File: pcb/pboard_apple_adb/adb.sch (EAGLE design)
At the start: 25 parts, among them IC3 STM32F042F4, SW1 324_SW, SW2 324_SW, SW4 324_SW

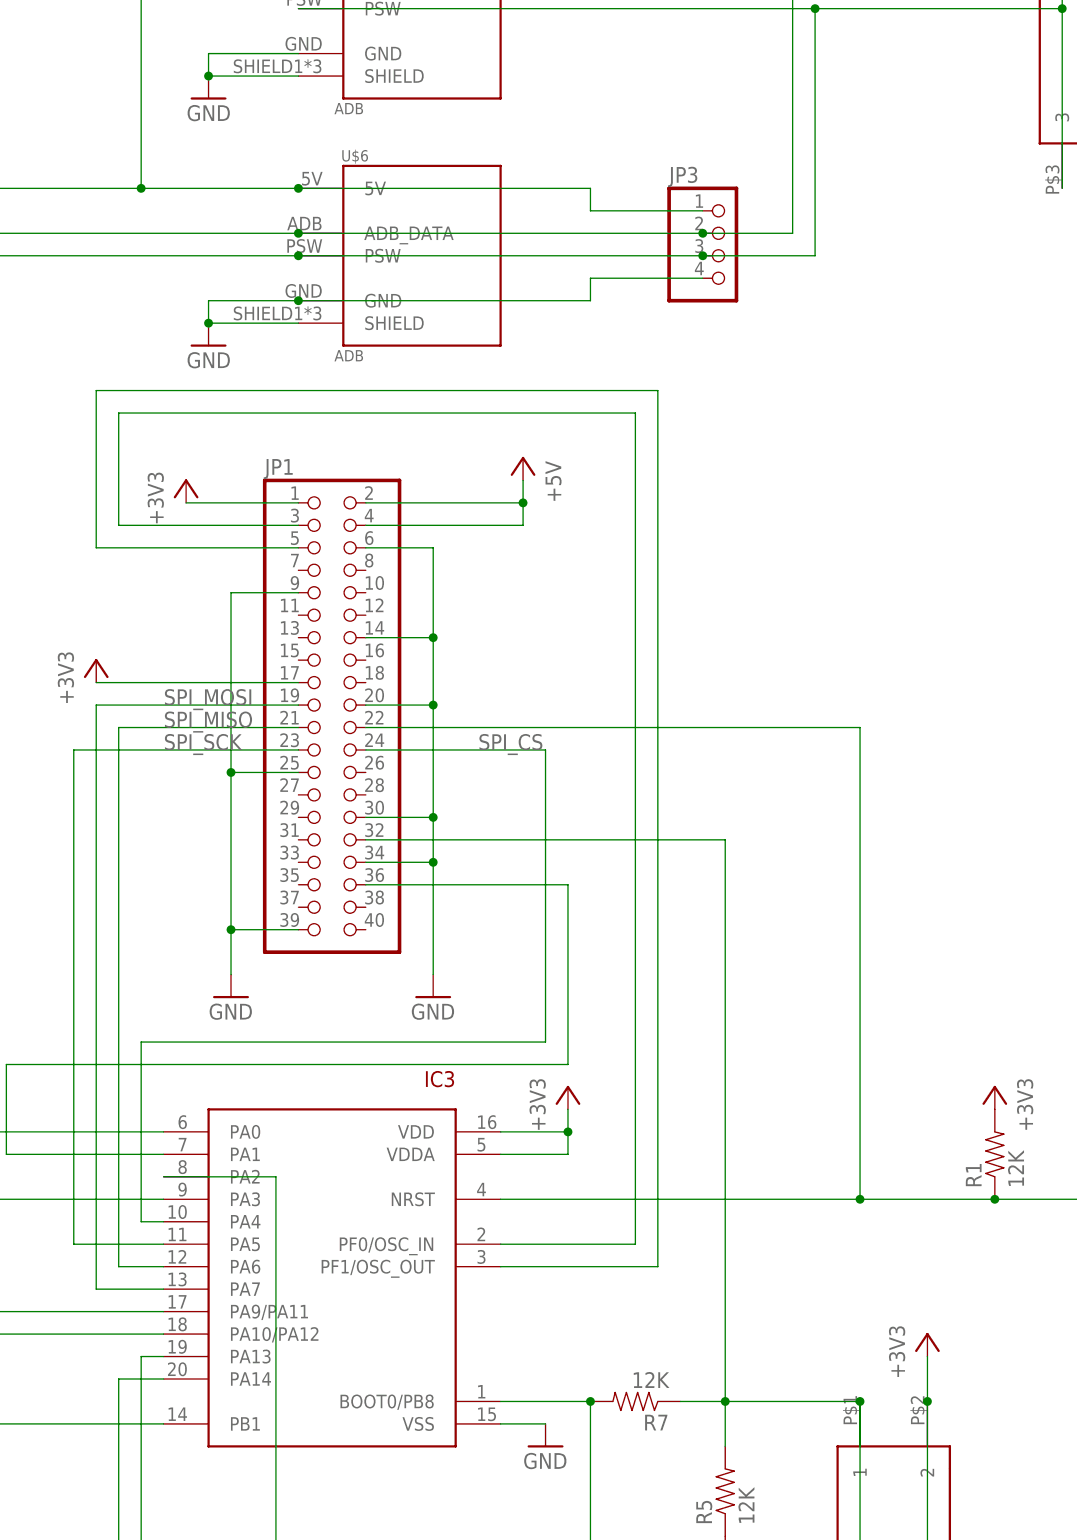
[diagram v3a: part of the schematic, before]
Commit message: updated PCB for second prototype run
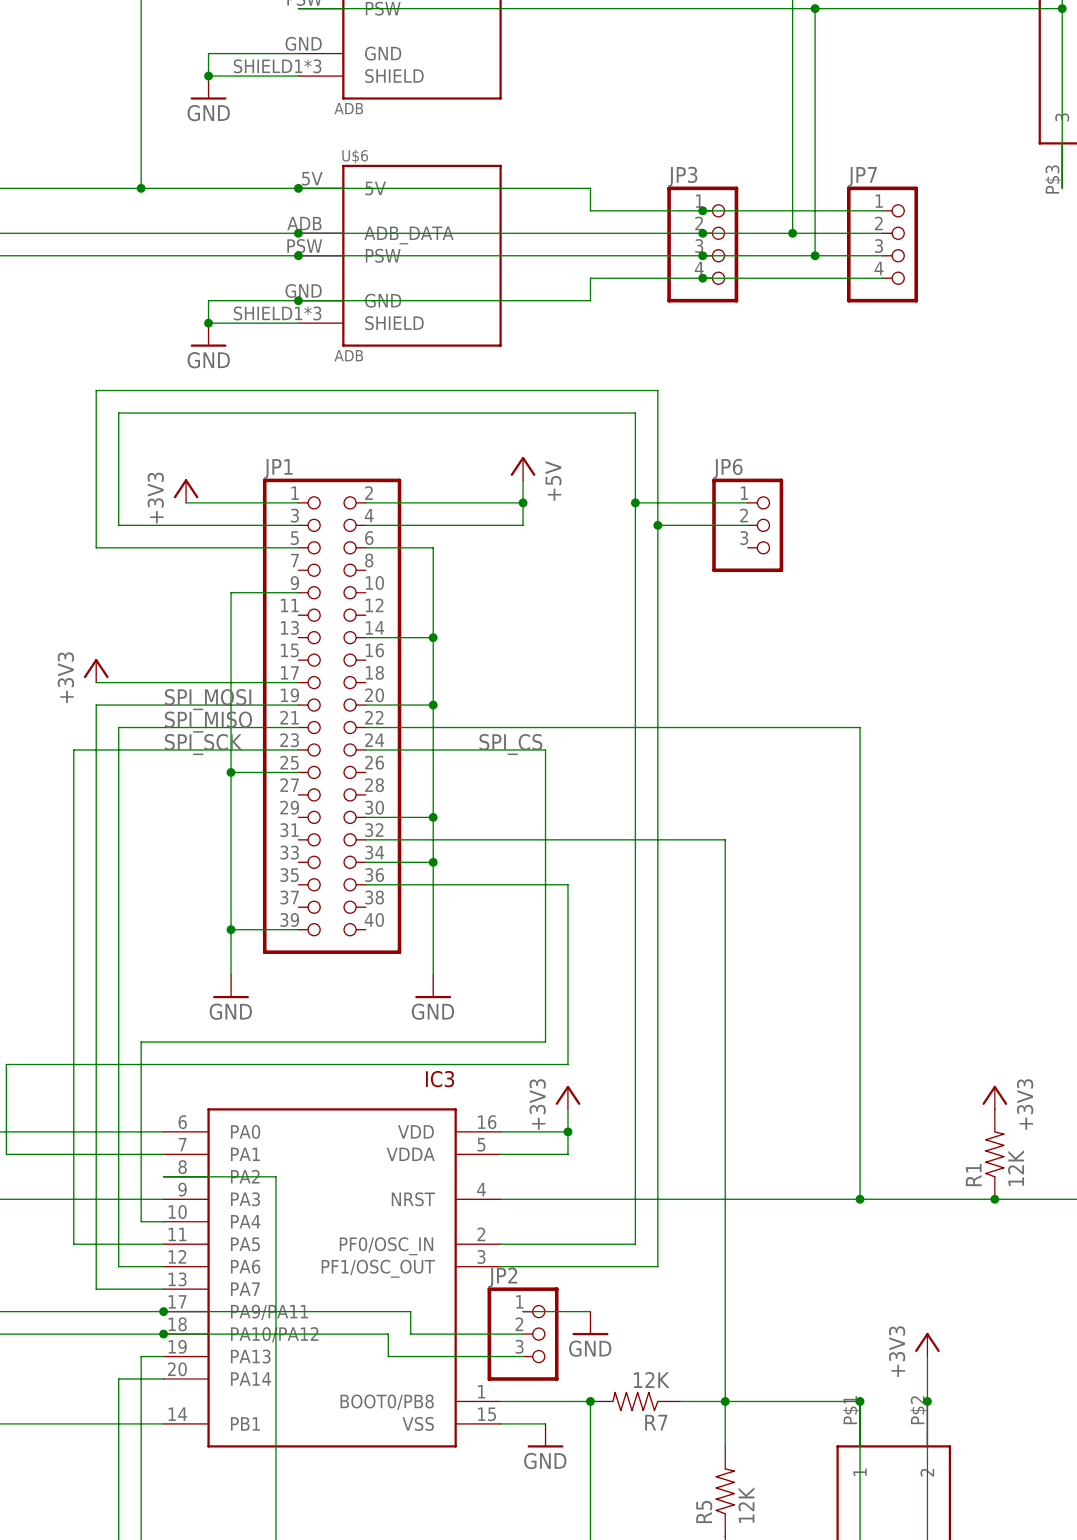
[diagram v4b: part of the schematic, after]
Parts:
- added JP2, JP6: (no value), pinhead:PINHD-1X3
- added JP7: (no value), pinhead:PINHD-1X4
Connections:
- net GND: now also JP2.1, JP7.4
- net N$10: now also JP6.1
- net N$11: now also JP6.2
- net N$14: now also JP7.1
- net N$15: now also JP7.2
- net N$18: now also JP7.3
- net N$3: now also JP2.3
- net N$4: now also JP2.2
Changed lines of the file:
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@@
 <part name="JP5" library="pinhead" library_urn="urn:adsk.eagle:library:325" deviceset="PINHD-1X5" device="" package3d_urn="urn:adsk.eagle:package:22469/2"/>
 <part name="R7" library="SparkFun-Passives" deviceset="RESISTOR" device="0805-RES" value="12K"/>
+<part name="JP2" library="pinhead" library_urn="urn:adsk.eagle:library:325" deviceset="PINHD-1X3" device="" package3d_urn="urn:adsk.eagle:package:22458/2"/>
+<part name="GND14" library="supply1" library_urn="urn:adsk.eagle:library:371" deviceset="GND" device=""/>
+<part name="JP6" library="pinhead" library_urn="urn:adsk.eagle:library:325" deviceset="PINHD-1X3" device="" package3d_urn="urn:adsk.eagle:package:22458/2"/>
+<part name="JP7" library="pinhead" library_urn="urn:adsk.eagle:library:325" deviceset="PINHD-1X4" device="" package3d_urn="urn:adsk.eagle:package:22407/2"/>
 </parts>
 <sheets>
@@
 <attribute name="NAME" x="138.43" y="-120.8786" size="1.778" layer="95" rot="R180"/>
 <attribute name="VALUE" x="138.43" y="-116.078" size="1.778" layer="96" rot="R180"/>
+</instance>
+<instance part="JP2" gate="A" x="124.46" y="-111.76" smashed="yes">
+<attribute name="NAME" x="118.11" y="-106.045" size="1.778" layer="95"/>
+<attribute name="VALUE" x="118.11" y="-119.38" size="1.778" layer="96"/>
+</instance>
+<instance part="GND14" gate="1" x="129.54" y="-111.76" smashed="yes">
+<attribute name="VALUE" x="127" y="-114.3" size="1.778" layer="96"/>
+</instance>
+<instance part="JP6" gate="A" x="149.86" y="-20.32" smashed="yes">
+<attribute name="NAME" x="143.51" y="-14.605" size="1.778" layer="95"/>
+<attribute name="VALUE" x="143.51" y="-27.94" size="1.778" layer="96"/>
+</instance>
+<instance part="JP7" gate="A" x="165.1" y="10.16" smashed="yes">
+<attribute name="NAME" x="158.75" y="18.415" size="1.778" layer="95"/>
+<attribute name="VALUE" x="158.75" y="2.54" size="1.778" layer="96"/>
 </instance>
 </instances>
@@
 <junction x="96.52" y="5.08"/>
 <junction x="86.36" y="2.54"/>
+<pinref part="JP7" gate="A" pin="4"/>
+<wire x1="142.24" y1="7.62" x2="162.56" y2="7.62" width="0.1524" layer="91"/>
+<junction x="142.24" y="7.62"/>
 </segment>
 <segment>
@@
 <wire x1="-2.54" y1="-60.96" x2="5.08" y2="-60.96" width="0.1524" layer="91"/>
 <junction x="-2.54" y="-60.96"/>
+</segment>
+<segment>
+<pinref part="JP2" gate="A" pin="1"/>
+<pinref part="GND14" gate="1" pin="GND"/>
+<wire x1="121.92" y1="-109.22" x2="129.54" y2="-109.22" width="0.1524" layer="91"/>
 </segment>
 </net>
@@
 <pinref part="J4" gate="J1" pin="D+"/>
 <wire x1="22.86" y1="-106.68" x2="5.08" y2="-106.68" width="0.1524" layer="91"/>
+<wire x1="81.28" y1="-111.76" x2="106.68" y2="-111.76" width="0.1524" layer="91"/>
+<wire x1="106.68" y1="-111.76" x2="106.68" y2="-114.3" width="0.1524" layer="91"/>
+<junction x="81.28" y="-111.76"/>
+<pinref part="JP2" gate="A" pin="3"/>
+<wire x1="106.68" y1="-114.3" x2="121.92" y2="-114.3" width="0.1524" layer="91"/>
 </segment>
 </net>
@@
 <pinref part="J4" gate="J1" pin="D-"/>
 <wire x1="81.28" y1="-109.22" x2="5.08" y2="-109.22" width="0.1524" layer="91"/>
+<wire x1="81.28" y1="-109.22" x2="109.22" y2="-109.22" width="0.1524" layer="91"/>
+<wire x1="109.22" y1="-109.22" x2="109.22" y2="-111.76" width="0.1524" layer="91"/>
+<junction x="81.28" y="-109.22"/>
+<pinref part="JP2" gate="A" pin="2"/>
+<wire x1="109.22" y1="-111.76" x2="121.92" y2="-111.76" width="0.1524" layer="91"/>
 </segment>
 </net>
@@
 <wire x1="76.2" y1="-20.32" x2="76.2" y2="-7.62" width="0.1524" layer="91"/>
 <wire x1="76.2" y1="-7.62" x2="134.62" y2="-7.62" width="0.1524" layer="91"/>
-<wire x1="134.62" y1="-7.62" x2="134.62" y2="-101.6" width="0.1524" layer="91"/>
+<wire x1="134.62" y1="-7.62" x2="134.62" y2="-17.78" width="0.1524" layer="91"/>
 <pinref part="IC3" gate="G$1" pin="PF0/OSC_IN"/>
+<wire x1="134.62" y1="-17.78" x2="134.62" y2="-101.6" width="0.1524" layer="91"/>
 <wire x1="134.62" y1="-101.6" x2="119.38" y2="-101.6" width="0.1524" layer="91"/>
+<pinref part="JP6" gate="A" pin="1"/>
+<wire x1="147.32" y1="-17.78" x2="134.62" y2="-17.78" width="0.1524" layer="91"/>
+<junction x="134.62" y="-17.78"/>
 </segment>
 </net>
@@
 <wire x1="73.66" y1="-22.86" x2="73.66" y2="-5.08" width="0.1524" layer="91"/>
 <wire x1="73.66" y1="-5.08" x2="137.16" y2="-5.08" width="0.1524" layer="91"/>
-<wire x1="137.16" y1="-5.08" x2="137.16" y2="-104.14" width="0.1524" layer="91"/>
+<wire x1="137.16" y1="-5.08" x2="137.16" y2="-20.32" width="0.1524" layer="91"/>
 <pinref part="IC3" gate="G$1" pin="PF1/OSC_OUT"/>
+<wire x1="137.16" y1="-20.32" x2="137.16" y2="-104.14" width="0.1524" layer="91"/>
 <wire x1="137.16" y1="-104.14" x2="119.38" y2="-104.14" width="0.1524" layer="91"/>
+<pinref part="JP6" gate="A" pin="2"/>
+<wire x1="147.32" y1="-20.32" x2="137.16" y2="-20.32" width="0.1524" layer="91"/>
+<junction x="137.16" y="-20.32"/>
 </segment>
 </net>
@@
 <pinref part="IC3" gate="G$1" pin="PA3"/>
 <wire x1="38.1" y1="-96.52" x2="81.28" y2="-96.52" width="0.1524" layer="91"/>
+<pinref part="JP7" gate="A" pin="1"/>
+<wire x1="142.24" y1="15.24" x2="162.56" y2="15.24" width="0.1524" layer="91"/>
+<junction x="142.24" y="15.24"/>
 </segment>
 </net>
@@
 <wire x1="45.72" y1="12.7" x2="96.52" y2="12.7" width="0.1524" layer="91"/>
 <junction x="96.52" y="12.7"/>
+<pinref part="JP7" gate="A" pin="2"/>
+<wire x1="152.4" y1="12.7" x2="162.56" y2="12.7" width="0.1524" layer="91"/>
+<junction x="152.4" y="12.7"/>
 </segment>
 </net>
@@
 <junction x="96.52" y="10.16"/>
 <junction x="154.94" y="38.1"/>
-</segment>
-</net>
+<pinref part="JP7" gate="A" pin="3"/>
+<wire x1="154.94" y1="10.16" x2="162.56" y2="10.16" width="0.1524" layer="91"/>
+<junction x="154.94" y="10.16"/>
+</segment>
+</net>

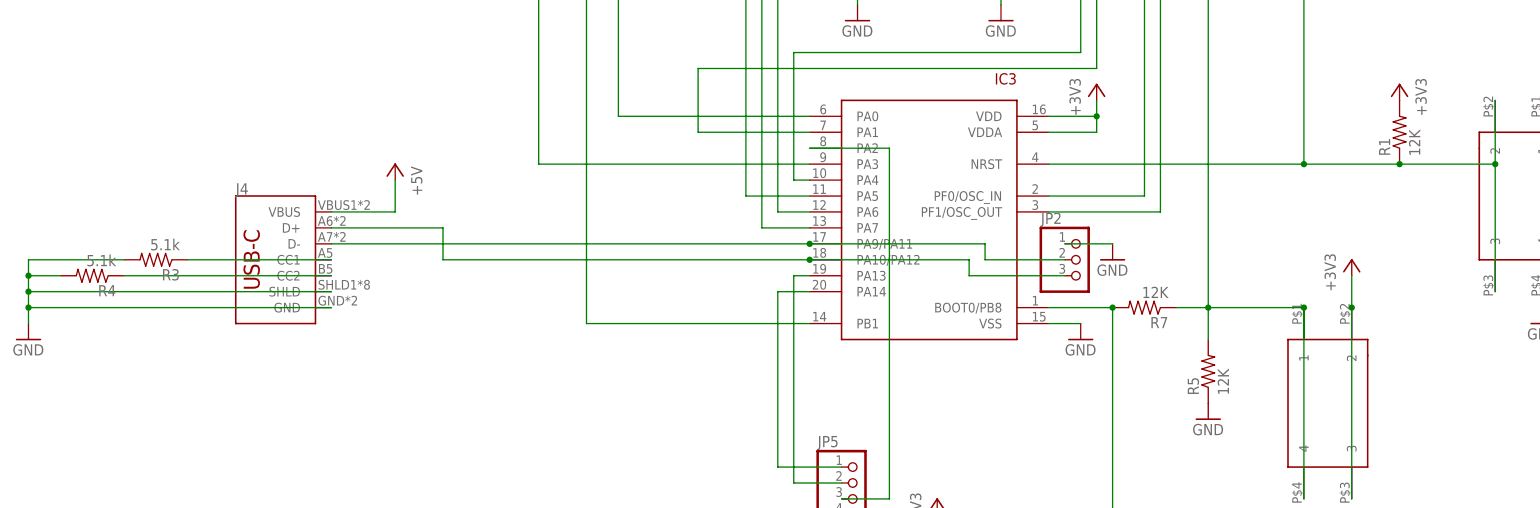
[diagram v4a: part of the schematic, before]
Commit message: updated component values
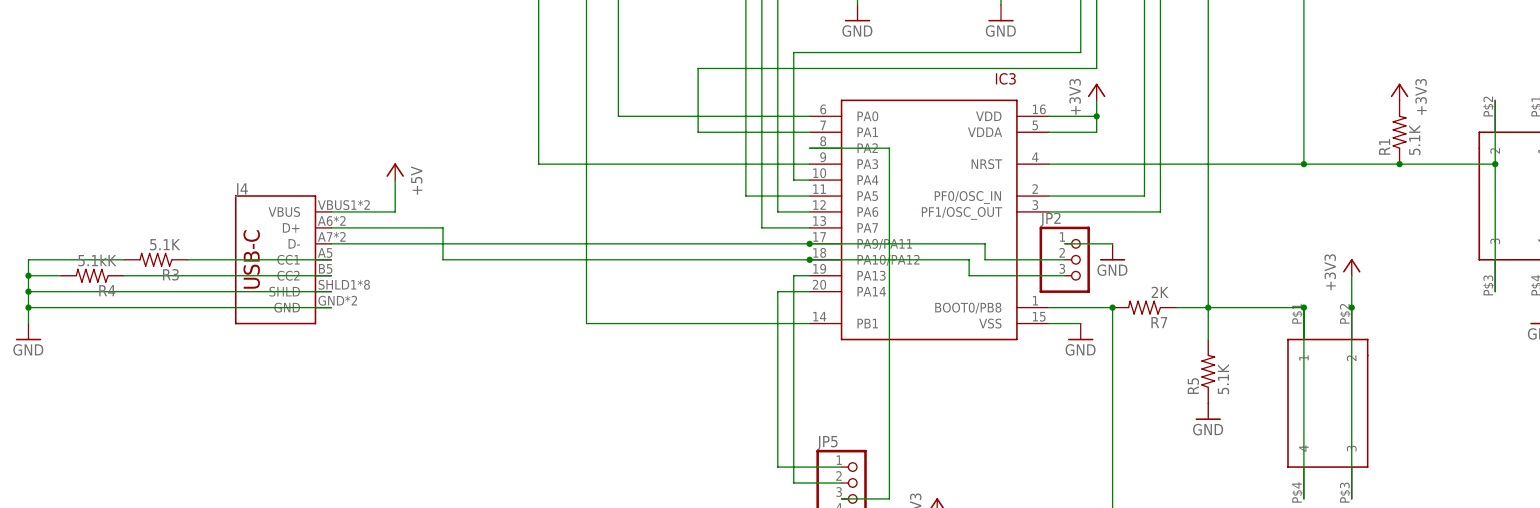
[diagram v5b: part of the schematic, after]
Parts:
- R1, R5: value 12K -> 5.1K
- R3: value 5.1k -> 5.1K
- R4: value 5.1k -> 5.1kK
- R7: value 12K -> 2K
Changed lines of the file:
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@@
 <part name="GND9" library="backplane" deviceset="GND" device=""/>
 <part name="GND8" library="supply1" deviceset="GND" device=""/>
-<part name="R1" library="SparkFun-Passives" deviceset="RESISTOR" device="0805-RES" value="12K"/>
+<part name="R1" library="SparkFun-Passives" deviceset="RESISTOR" device="0805-RES" value="5.1K"/>
 <part name="+3V4" library="supply1" library_urn="urn:adsk.eagle:library:371" deviceset="+3V3" device=""/>
 <part name="+3V10" library="backplane" deviceset="+3V3" device=""/>
 <part name="J4" library="SparkFun-Connectors" deviceset="USB_C" device="16PIN"/>
-<part name="R3" library="SparkFun-Passives" deviceset="RESISTOR" device="0805-RES" value="5.1k"/>
-<part name="R4" library="SparkFun-Passives" deviceset="RESISTOR" device="0805-RES" value="5.1k"/>
+<part name="R3" library="SparkFun-Passives" deviceset="RESISTOR" device="0805-RES" value="5.1K"/>
+<part name="R4" library="SparkFun-Passives" deviceset="RESISTOR" device="0805-RES" value="5.1kK"/>
 <part name="GND4" library="supply1" library_urn="urn:adsk.eagle:library:371" deviceset="GND" device=""/>
 <part name="SW1" library="3pos_slide_switch_centered" deviceset="324_SW" device="" value="324_SW"/>
-<part name="R5" library="SparkFun-Passives" deviceset="RESISTOR" device="0805-RES" value="12K"/>
+<part name="R5" library="SparkFun-Passives" deviceset="RESISTOR" device="0805-RES" value="5.1K"/>
 <part name="GND6" library="supply1" library_urn="urn:adsk.eagle:library:371" deviceset="GND" device=""/>
 <part name="C8" library="clock" deviceset="CAP" device="0805" value="100nF"/>
@@
 <part name="+3V13" library="supply1" library_urn="urn:adsk.eagle:library:371" deviceset="+3V3" device=""/>
 <part name="JP5" library="pinhead" library_urn="urn:adsk.eagle:library:325" deviceset="PINHD-1X5" device="" package3d_urn="urn:adsk.eagle:package:22469/2"/>
-<part name="R7" library="SparkFun-Passives" deviceset="RESISTOR" device="0805-RES" value="12K"/>
+<part name="R7" library="SparkFun-Passives" deviceset="RESISTOR" device="0805-RES" value="2K"/>
 <part name="JP2" library="pinhead" library_urn="urn:adsk.eagle:library:325" deviceset="PINHD-1X3" device="" package3d_urn="urn:adsk.eagle:package:22458/2"/>
 <part name="GND14" library="supply1" library_urn="urn:adsk.eagle:library:371" deviceset="GND" device=""/>
